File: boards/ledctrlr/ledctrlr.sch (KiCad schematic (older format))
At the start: 54 parts, among them IC1 ATMEGA168-P, IC2 SN75176B, J1 RJ45, J2 RJ45, SW1 SW_PUSH, U1 LM7805, X1 CRYSTAL

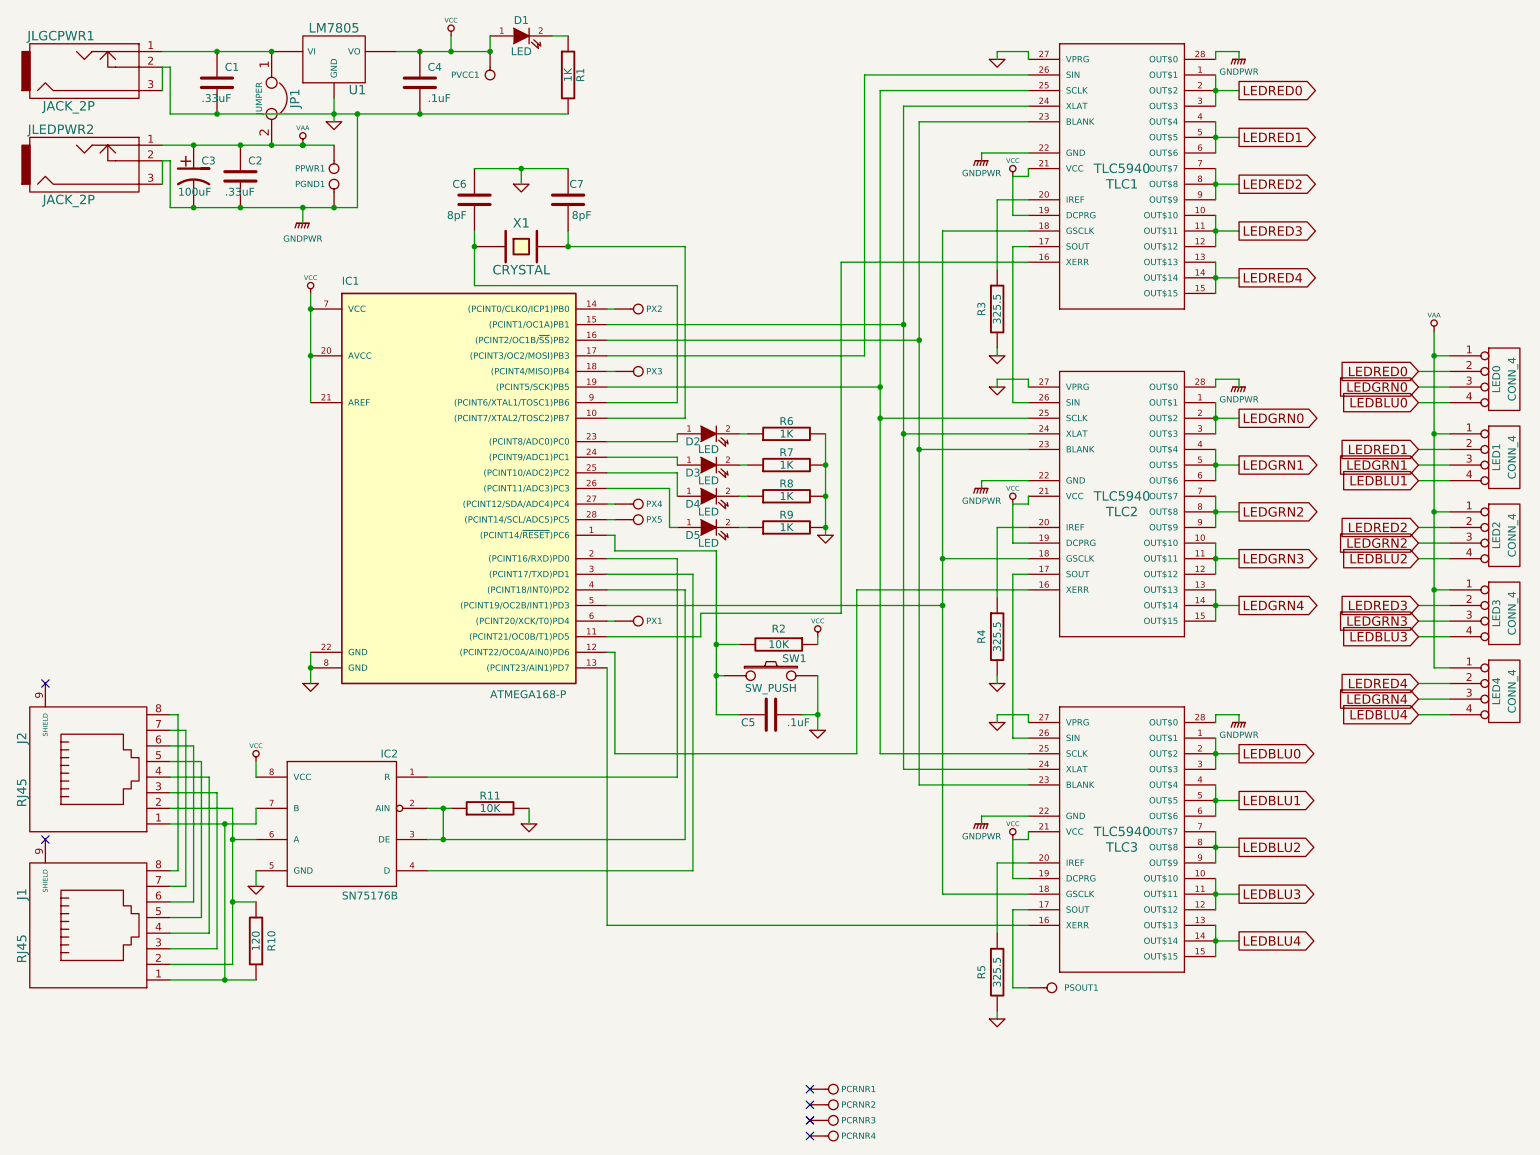
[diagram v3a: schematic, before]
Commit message: fixed smd tlc5940s
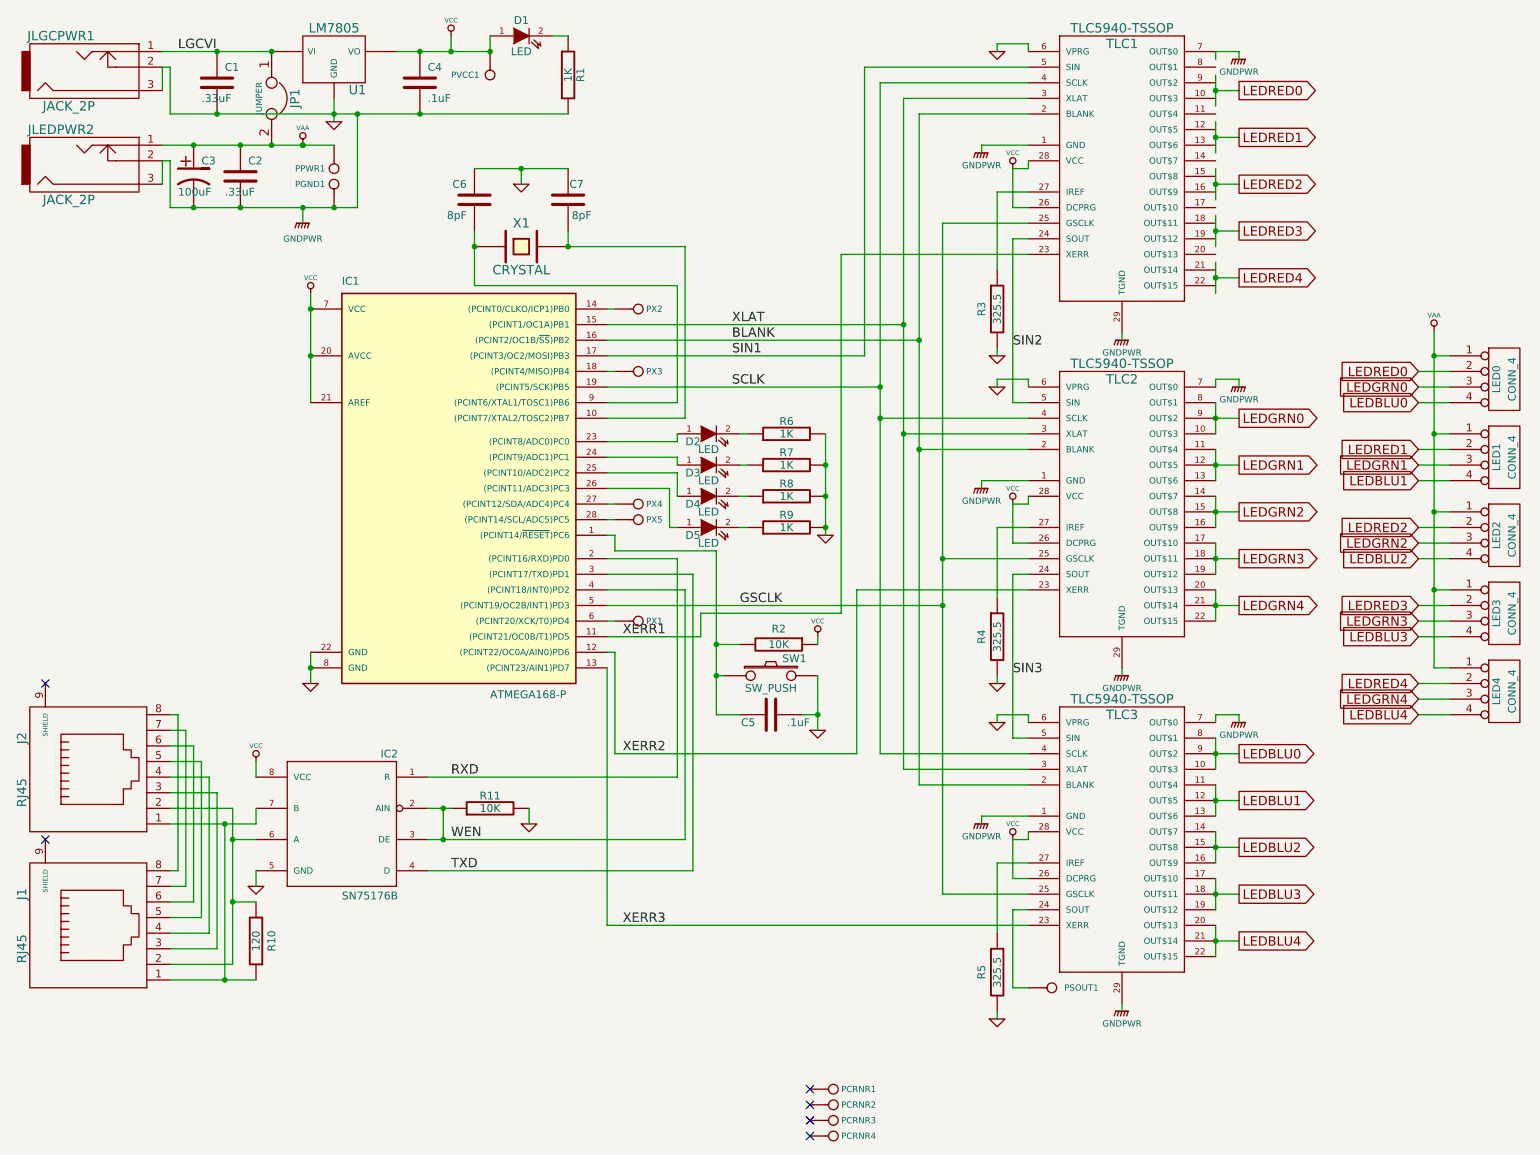
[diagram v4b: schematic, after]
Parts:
- removed TLC1, TLC2, TLC3: TLC5940, tssop-28-thermal, symbol TLC5940
- added TLC1, TLC2, TLC3: TLC5940-TSSOP, tlc5940-tssop, symbol TLC5940-TSSOP
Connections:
- net labels added: BLANK, GSCLK, LGCVI, RXD, SCLK, SIN1, SIN2, SIN3, TXD, WEN, XERR1, XERR2, XERR3, XLAT
- wire segments 239 -> 242
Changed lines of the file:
@@
-EESchema Schematic File Version 2  date Sun 25 Mar 2012 02:40:29 PM EDT
+EESchema Schematic File Version 2  date Tue 27 Mar 2012 04:43:19 PM EDT
 LIBS:power
 LIBS:device
@@
 LIBS:sn75176b
 LIBS:SparkFun
+LIBS:tlc5940-tssop
 LIBS:ledctrlr-cache
 EELAYER 25  0
@@
 Sheet 1 1
 Title "5-RGB LED Controller Board"
-Date "25 mar 2012"
+Date "27 mar 2012"
 Rev "2.0"
 Comp "J. Colosimo"
@@
 Comment4 ""
 $EndDescr
-$Comp
-L TLC5940 TLC1
-U 1 1 4D1A4475
-P 7800 1600
-F 0 "TLC1" H 7800 1500 60  0000 C CNN
-F 1 "TLC5940" H 7800 1600 60  0000 C CNN
-F 2 "tssop-28-thermal" H 7800 1600 60  0001 C CNN
-F 4 "TLC5940NT" H 7800 1600 60  0001 C CNN "Part"
-F 5 "296-17732-5-ND" H 7800 1600 60  0001 C CNN "DigikeyPart"
-	1    7800 1600
-	-1   0    0    -1
-$EndComp
 $Comp
 L GND #PWR01
@@
 L GNDPWR #PWR012
 U 1 1 4D346371
-P 6900 1550
-F 0 "#PWR012" H 6900 1600 40  0001 C CNN
-F 1 "GNDPWR" H 6900 1470 40  0000 C CNN
-	1    6900 1550
+P 6900 1500
+F 0 "#PWR012" H 6900 1550 40  0001 C CNN
+F 1 "GNDPWR" H 6900 1420 40  0000 C CNN
+	1    6900 1500
 	1    0    0    -1
 $EndComp
@@
 L GND #PWR017
 U 1 1 4D33DDCE
-P 7000 900
-F 0 "#PWR017" H 7000 900 30  0001 C CNN
-F 1 "GND" H 7000 830 30  0001 C CNN
-	1    7000 900
+P 7000 850
+F 0 "#PWR017" H 7000 850 30  0001 C CNN
+F 1 "GND" H 7000 780 30  0001 C CNN
+	1    7000 850
 	1    0    0    -1
 $EndComp
@@
 $EndComp
 $Comp
-L TLC5940 TLC?
-U 1 1 4D1A46AA
-P 7800 5850
-AR Path="/4D1A4475" Ref="TLC?"  Part="1"
-AR Path="/4D1A46AA" Ref="TLC3"  Part="1"
-F 0 "TLC3" H 7800 5750 60  0000 C CNN
-F 1 "TLC5940" H 7800 5850 60  0000 C CNN
-F 2 "tssop-28-thermal" H 7800 5850 60  0001 C CNN
-F 4 "TLC5940NT" H 7800 5850 60  0001 C CNN "Part"
-F 5 "296-17732-5-ND" H 7800 5850 60  0001 C CNN "DigikeyPart"
-	1    7800 5850
-	-1   0    0    -1
-$EndComp
-$Comp
-L TLC5940 TLC?
-U 1 1 4D1A469F
-P 7800 3700
-AR Path="/4D1A4475" Ref="TLC?"  Part="1"
-AR Path="/4D1A469F" Ref="TLC2"  Part="1"
-F 0 "TLC2" H 7800 3600 60  0000 C CNN
-F 1 "TLC5940" H 7800 3700 60  0000 C CNN
-F 2 "tssop-28-thermal" H 7740 3540 60  0001 C CNN
-F 4 "TLC5940NT" H 7800 3700 60  0001 C CNN "Part"
-F 5 "296-17732-5-ND" H 7800 3700 60  0001 C CNN "DigikeyPart"
-	1    7800 3700
-	-1   0    0    -1
-$EndComp
-$Comp
 L R R4
 U 1 1 4D1A469E
@@
 L VCC #PWR027
 U 1 1 4D1A459E
-P 7100 1650
-F 0 "#PWR027" H 7100 1750 30  0001 C CNN
-F 1 "VCC" H 7100 1750 30  0000 C CNN
-	1    7100 1650
+P 7100 1600
+F 0 "#PWR027" H 7100 1700 30  0001 C CNN
+F 1 "VCC" H 7100 1700 30  0000 C CNN
+	1    7100 1600
 	1    0    0    -1
 $EndComp
@@
 	-1   0    0    1
 $EndComp
+$Comp
+L CONN_1 PPWR1
+U 1 1 4F6E48D8
+P 2750 1600
+F 0 "PPWR1" V 2750 1350 40  0000 L CNN
+F 1 "CONN_1" H 2750 1655 30  0001 C CNN
+F 2 "PAD" H 2750 1755 30  0001 C CNN
+	1    2750 1600
+	0    1    1    0
+$EndComp
+$Comp
+L CONN_1 PVCC1
+U 1 1 4F6E4A82
+P 3750 1000
+F 0 "PVCC1" V 3750 750 40  0000 L CNN
+F 1 "CONN_1" H 3750 1055 30  0001 C CNN
+F 2 "PAD" H 3750 1155 30  0001 C CNN
+	1    3750 1000
+	0    1    1    0
+$EndComp
+$Comp
+L TLC5940-TSSOP TLC1
+U 1 1 4F71FDED
+P 7800 1550
+F 0 "TLC1" H 7800 2300 60  0000 C CNN
+F 1 "TLC5940-TSSOP" H 7800 2400 60  0000 C CNN
+F 2 "tlc5940-tssop" H 7800 1550 60  0001 C CNN
+	1    7800 1550
+	-1   0    0    -1
+$EndComp
+$Comp
+L TLC5940-TSSOP TLC2
+U 1 1 4F71FE3B
+P 7800 3700
+F 0 "TLC2" H 7800 4450 60  0000 C CNN
+F 1 "TLC5940-TSSOP" H 7800 4550 60  0000 C CNN
+F 2 "tlc5940-tssop" H 7800 3700 60  0001 C CNN
+	1    7800 3700
+	-1   0    0    -1
+$EndComp
+$Comp
+L TLC5940-TSSOP TLC3
+U 1 1 4F71FE41
+P 7800 5850
+F 0 "TLC3" H 7800 6600 60  0000 C CNN
+F 1 "TLC5940-TSSOP" H 7800 6700 60  0000 C CNN
+F 2 "tlc5940-tssop" H 7800 5850 60  0001 C CNN
+	1    7800 5850
+	-1   0    0    -1
+$EndComp
+Text Label 5300 2800 0    60   ~ 0
+SIN1
+Text Label 5300 3000 0    60   ~ 0
+SCLK
+Text Label 5300 2600 0    60   ~ 0
+XLAT
+Text Label 5300 2700 0    60   ~ 0
+BLANK
+Text Label 5350 4400 0    60   ~ 0
+GSCLK
+Text Label 4600 4600 0    60   ~ 0
+XERR1
+Text Label 4600 5350 0    60   ~ 0
+XERR2
+Text Label 4600 6450 0    60   ~ 0
+XERR3
+Text Label 3500 5500 0    60   ~ 0
+RXD
+Text Label 3500 6100 0    60   ~ 0
+TXD
+Text Label 3500 5900 0    60   ~ 0
+WEN
+Text Label 1750 850  0    60   ~ 0
+LGCVI
+Text Label 7100 2750 0    60   ~ 0
+SIN2
+Text Label 7100 4850 0    60   ~ 0
+SIN3
+$Comp
+L GNDPWR #PWR?
+U 1 1 4F722628
+P 7800 2700
+F 0 "#PWR?" H 7800 2750 40  0001 C CNN
+F 1 "GNDPWR" H 7800 2620 40  0000 C CNN
+	1    7800 2700
+	1    0    0    -1
+$EndComp
+$Comp
+L GNDPWR #PWR?
+U 1 1 4F722891
+P 7800 4850
+F 0 "#PWR?" H 7800 4900 40  0001 C CNN
+F 1 "GNDPWR" H 7800 4770 40  0000 C CNN
+	1    7800 4850
+	1    0    0    -1
+$EndComp
+$Comp
+L GNDPWR #PWR?
+U 1 1 4F72383A
+P 7800 7000
+F 0 "#PWR?" H 7800 7050 40  0001 C CNN
+F 1 "GNDPWR" H 7800 6920 40  0000 C CNN
+	1    7800 7000
+	1    0    0    -1
+$EndComp
 Wire Wire Line
 	1700 1550 1700 1850
@@
 	5350 3300 5400 3300
 Wire Wire Line
-	7200 1800 7000 1800
+	7200 1750 7000 1750
 Wire Wire Line
 	4250 2000 4250 2100
@@
 	8550 900  8550 850
 Wire Wire Line
-	7200 900  7200 850
-Wire Wire Line
 	6900 3650 6900 3600
 Wire Wire Line
 	4500 2800 6150 2800
 Wire Wire Line
-	6150 2800 6150 1000
+	6150 2800 6150 950
 Wire Wire Line
 	7200 6850 7100 6850
@@
 	7100 6350 7200 6350
 Wire Wire Line
-	7200 2100 7100 2100
-Wire Wire Line
-	7100 2100 7100 3100
+	7200 2050 7100 2050
+Wire Wire Line
+	7100 2050 7100 3100
 Wire Wire Line
 	7100 3100 7200 3100
@@
 	7200 5750 6900 5750
 Wire Wire Line
-	7200 1500 6900 1500
+	7200 1450 6900 1450
 Connection ~ 6400 2600
 Wire Wire Line
@@
 	4500 4400 6650 4400
 Wire Wire Line
-	6150 1000 7200 1000
+	6150 950  7200 950
 Wire Wire Line
 	6250 3200 7200 3200
 Wire Wire Line
-	7200 1100 6250 1100
+	7200 1050 6250 1050
 Connection ~ 6500 3400
 Wire Wire Line
@@
 	7200 6250 6650 6250
 Wire Wire Line
-	6650 6250 6650 2000
-Wire Wire Line
-	7100 1900 7100 1650
-Wire Wire Line
-	7100 1900 7200 1900
+	6650 6250 6650 1950
+Wire Wire Line
+	7100 1850 7100 1600
+Wire Wire Line
+	7100 1850 7200 1850
 Wire Wire Line
 	8550 850  8400 850
@@
 	2050 5800 2050 6800
 Wire Wire Line
-	7200 850  7000 850
-Wire Wire Line
-	7000 1800 7000 2250
+	7000 1750 7000 2250
 Wire Wire Line
 	8400 1000 8400 1200
@@
 Connection ~ 8400 2300
 Wire Wire Line
-	7200 1600 7200 1650
-Wire Wire Line
-	7200 1650 7100 1650
-Wire Wire Line
 	7200 3750 7100 3750
 Wire Wire Line
@@
 	7100 6150 7100 5900
 Wire Wire Line
-	6650 2000 7200 2000
+	6650 1950 7200 1950
 Wire Wire Line
 	7200 4100 6650 4100
 Wire Wire Line
-	7200 1300 6500 1300
+	7200 1250 6500 1250
 Wire Wire Line
 	7200 5550 6500 5550
 Wire Wire Line
-	6500 5550 6500 1300
+	6500 5550 6500 1250
 Wire Wire Line
 	7200 5450 6400 5450
 Wire Wire Line
-	7200 1200 6400 1200
-Wire Wire Line
-	6250 1100 6250 5350
+	7200 1150 6400 1150
+Wire Wire Line
+	6250 1050 6250 5350
 Wire Wire Line
 	6250 5350 7200 5350
@@
 Connection ~ 3950 1600
 Wire Wire Line
-	6900 1500 6900 1550
+	6900 1450 6900 1500
 Wire Wire Line
 	6900 5750 6900 5800
 Wire Wire Line
-	7000 850  7000 900
-Wire Wire Line
 	7000 2950 7000 3000
 Wire Wire Line
@@
 	6250 3000 4500 3000
 Wire Wire Line
-	6400 1200 6400 5450
+	6400 1150 6400 5450
 Wire Wire Line
 	2600 4900 2600 4700
@@
 	4500 6450 4500 4800
 Wire Wire Line
-	7200 2200 6000 2200
-Wire Wire Line
-	6000 2200 6000 4450
+	7200 2150 6000 2150
+Wire Wire Line
+	6000 2150 6000 4450
 Wire Wire Line
 	6000 4450 5100 4450
@@
 Connection ~ 2550 1450
 Connection ~ 2550 1450
-$Comp
-L CONN_1 PPWR1
-U 1 1 4F6E48D8
-P 2750 1600
-F 0 "PPWR1" V 2750 1350 40  0000 L CNN
-F 1 "CONN_1" H 2750 1655 30  0001 C CNN
-F 2 "PAD" H 2750 1755 30  0001 C CNN
-	1    2750 1600
-	0    1    1    0
-$EndComp
-$Comp
-L CONN_1 PVCC1
-U 1 1 4F6E4A82
-P 3750 1000
-F 0 "PVCC1" V 3750 750 40  0000 L CNN
-F 1 "CONN_1" H 3750 1055 30  0001 C CNN
-F 2 "PAD" H 3750 1155 30  0001 C CNN
-	1    3750 1000
-	0    1    1    0
-$EndComp
 Connection ~ 3750 850
+Wire Wire Line
+	7000 850  7000 800
+Wire Wire Line
+	7000 800  7200 800
+Wire Wire Line
+	7200 800  7200 850
+Wire Wire Line
+	7100 1600 7200 1600
+Wire Wire Line
+	7200 1600 7200 1550
+Wire Wire Line
+	7800 2650 7800 2700
+Wire Wire Line
+	7800 4800 7800 4850
+Wire Wire Line
+	7800 6950 7800 7000
 $EndSCHEMATC

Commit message: working on board layout moar
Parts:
- TLC1, TLC2, TLC3: footprint tlc5940-tssop -> tssop-28-thermal
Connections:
- net labels added: DBG0, DBG1, DBG2, DBG3, DIFFA, DIFFB, IREF1, IREF2, IREF3, RESET, RJ3, RJ4, RJ5, RJ6, RJ7, RJ8, SOUT, XPB0, XPB4, XPC4, XPC5, XPD4, XTAL1, XTAL2
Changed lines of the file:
@@
-EESchema Schematic File Version 2  date Tue 27 Mar 2012 04:43:19 PM EDT
+EESchema Schematic File Version 2  date Sat 31 Mar 2012 01:44:57 AM EDT
 LIBS:power
 LIBS:device
@@
 Sheet 1 1
 Title "5-RGB LED Controller Board"
-Date "27 mar 2012"
+Date "31 mar 2012"
 Rev "2.0"
 Comp "J. Colosimo"
@@
 L GNDPWR #PWR011
 U 1 1 4D346394
-P 8550 900
-F 0 "#PWR011" H 8550 950 40  0001 C CNN
-F 1 "GNDPWR" H 8550 820 40  0000 C CNN
-	1    8550 900
+P 8550 850
+F 0 "#PWR011" H 8550 900 40  0001 C CNN
+F 1 "GNDPWR" H 8550 770 40  0000 C CNN
+	1    8550 850
 	1    0    0    -1
 $EndComp
@@
 	1    0    0    -1
 $EndComp
-Text GLabel 8550 1100 2    60   Output ~ 0
+Text GLabel 8550 1050 2    60   Output ~ 0
 LEDRED0
-Text GLabel 8550 1400 2    60   Output ~ 0
+Text GLabel 8550 1350 2    60   Output ~ 0
 LEDRED1
-Text GLabel 8550 1700 2    60   Output ~ 0
+Text GLabel 8550 1650 2    60   Output ~ 0
 LEDRED2
-Text GLabel 8550 2000 2    60   Output ~ 0
+Text GLabel 8550 1950 2    60   Output ~ 0
 LEDRED3
-Text GLabel 8550 2300 2    60   Output ~ 0
+Text GLabel 8550 2250 2    60   Output ~ 0
 LEDRED4
 Text GLabel 8550 3200 2    60   Output ~ 0
@@
 F 0 "TLC1" H 7800 2300 60  0000 C CNN
 F 1 "TLC5940-TSSOP" H 7800 2400 60  0000 C CNN
-F 2 "tlc5940-tssop" H 7800 1550 60  0001 C CNN
+F 2 "tssop-28-thermal" H 7800 1550 60  0001 C CNN
 	1    7800 1550
 	-1   0    0    -1
@@
 F 0 "TLC2" H 7800 4450 60  0000 C CNN
 F 1 "TLC5940-TSSOP" H 7800 4550 60  0000 C CNN
-F 2 "tlc5940-tssop" H 7800 3700 60  0001 C CNN
+F 2 "tssop-28-thermal" H 7800 3700 60  0001 C CNN
 	1    7800 3700
 	-1   0    0    -1
@@
 F 0 "TLC3" H 7800 6600 60  0000 C CNN
 F 1 "TLC5940-TSSOP" H 7800 6700 60  0000 C CNN
-F 2 "tlc5940-tssop" H 7800 5850 60  0001 C CNN
+F 2 "tssop-28-thermal" H 7800 5850 60  0001 C CNN
 	1    7800 5850
 	-1   0    0    -1
@@
 SIN3
 $Comp
-L GNDPWR #PWR?
+L GNDPWR #PWR030
 U 1 1 4F722628
 P 7800 2700
-F 0 "#PWR?" H 7800 2750 40  0001 C CNN
+F 0 "#PWR030" H 7800 2750 40  0001 C CNN
 F 1 "GNDPWR" H 7800 2620 40  0000 C CNN
 	1    7800 2700
@@
 $EndComp
 $Comp
-L GNDPWR #PWR?
+L GNDPWR #PWR031
 U 1 1 4F722891
 P 7800 4850
-F 0 "#PWR?" H 7800 4900 40  0001 C CNN
+F 0 "#PWR031" H 7800 4900 40  0001 C CNN
 F 1 "GNDPWR" H 7800 4770 40  0000 C CNN
 	1    7800 4850
@@
 $EndComp
 $Comp
-L GNDPWR #PWR?
+L GNDPWR #PWR032
 U 1 1 4F72383A
 P 7800 7000
-F 0 "#PWR?" H 7800 7050 40  0001 C CNN
+F 0 "#PWR032" H 7800 7050 40  0001 C CNN
 F 1 "GNDPWR" H 7800 6920 40  0000 C CNN
 	1    7800 7000
@@
 	7000 2800 7000 2750
 Wire Wire Line
-	8550 900  8550 850
+	8550 850  8550 800
 Wire Wire Line
 	6900 3650 6900 3600
@@
 	7100 1850 7200 1850
 Wire Wire Line
-	8550 850  8400 850
-Wire Wire Line
-	8400 850  8400 900
+	8550 800  8400 800
 Connection ~ 2600 2500
 Wire Wire Line
@@
 Wire Wire Line
 	7000 1750 7000 2250
-Wire Wire Line
-	8400 1000 8400 1200
-Connection ~ 8400 1100
-Wire Wire Line
-	8400 1300 8400 1500
-Connection ~ 8400 1400
-Wire Wire Line
-	8400 1600 8400 1800
-Connection ~ 8400 1700
-Wire Wire Line
-	8400 1900 8400 2100
-Connection ~ 8400 2000
-Wire Wire Line
-	8400 2200 8400 2400
-Connection ~ 8400 2300
 Wire Wire Line
 	7200 3750 7100 3750
@@
 Connection ~ 9800 4300
 Wire Wire Line
-	8400 1100 8550 1100
-Wire Wire Line
-	8400 1400 8550 1400
-Wire Wire Line
-	8400 1700 8550 1700
-Wire Wire Line
-	8400 2000 8550 2000
-Wire Wire Line
-	8400 2300 8550 2300
+	8550 1050 8400 1050
+Wire Wire Line
+	8550 1350 8400 1350
+Wire Wire Line
+	8550 1650 8400 1650
+Wire Wire Line
+	8550 1950 8400 1950
+Wire Wire Line
+	8550 2250 8400 2250
 Wire Wire Line
 	8400 3200 8550 3200
@@
 Wire Wire Line
 	7800 6950 7800 7000
+Wire Wire Line
+	8400 800  8400 850
+Wire Wire Line
+	8400 950  8400 1150
+Connection ~ 8400 1050
+Connection ~ 8400 1050
+Wire Wire Line
+	8400 1250 8400 1450
+Connection ~ 8400 1350
+Wire Wire Line
+	8400 1550 8400 1750
+Connection ~ 8400 1650
+Wire Wire Line
+	8400 1850 8400 2050
+Connection ~ 8400 1950
+Wire Wire Line
+	8400 2150 8400 2350
+Connection ~ 8400 2250
+Text Label 7000 1850 2    60   ~ 0
+IREF1
+Text Label 7000 4000 2    60   ~ 0
+IREF2
+Text Label 7000 6150 2    60   ~ 0
+IREF3
+Text Label 1750 6700 0    60   ~ 0
+DIFFA
+Text Label 1750 6800 0    60   ~ 0
+DIFFB
+Text Label 2000 5650 0    60   ~ 0
+RJ3
+Text Label 1950 5550 0    60   ~ 0
+RJ4
+Text Label 1900 5450 0    60   ~ 0
+RJ5
+Text Label 1800 5250 0    60   ~ 0
+RJ7
+Text Label 1750 5150 0    60   ~ 0
+RJ8
+Text Label 1850 5350 0    60   ~ 0
+RJ6
+Text Label 4700 2350 0    60   ~ 0
+XTAL1
+Text Label 4700 2100 0    60   ~ 0
+XTAL2
+Text Label 4500 2500 0    60   ~ 0
+XPB0
+Text Label 4500 2900 0    60   ~ 0
+XPB4
+Text Label 4500 3750 0    60   ~ 0
+XPC4
+Text Label 4500 3850 0    60   ~ 0
+XPC5
+Text Label 4500 4500 0    60   ~ 0
+XPD4
+Text Label 5200 4200 0    60   ~ 0
+RESET
+Text Label 4600 3350 0    60   ~ 0
+DBG0
+Text Label 4600 3450 0    60   ~ 0
+DBG1
+Text Label 4600 3550 0    60   ~ 0
+DBG2
+Text Label 4600 3650 0    60   ~ 0
+DBG3
+Text Label 7100 6750 0    60   ~ 0
+SOUT
 $EndSCHEMATC
